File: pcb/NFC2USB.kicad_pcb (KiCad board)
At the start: 4 copper layers, 39 x 40 mm, 44 parts, among them J1 USB_C_USB2.0, SW1 BOOTSEL, SW2 MODE, U1 NFCModuleRC522, U2 AMS1117-3.3, U3 W25Q32JVSS, U4 RP2040, Y1 12MHz

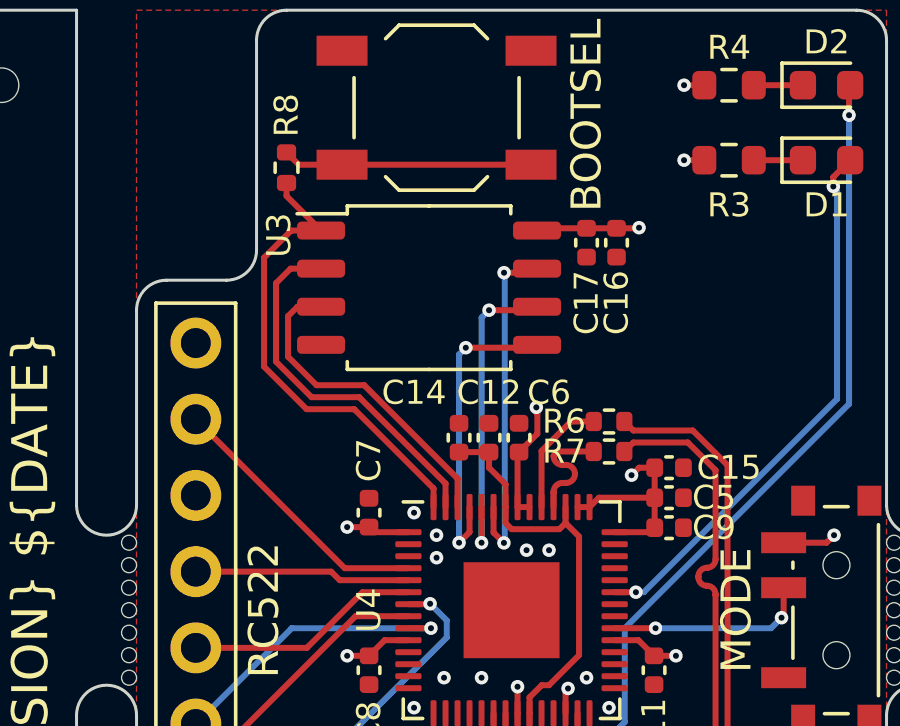
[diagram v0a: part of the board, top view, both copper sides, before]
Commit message: feat: change flash footprint
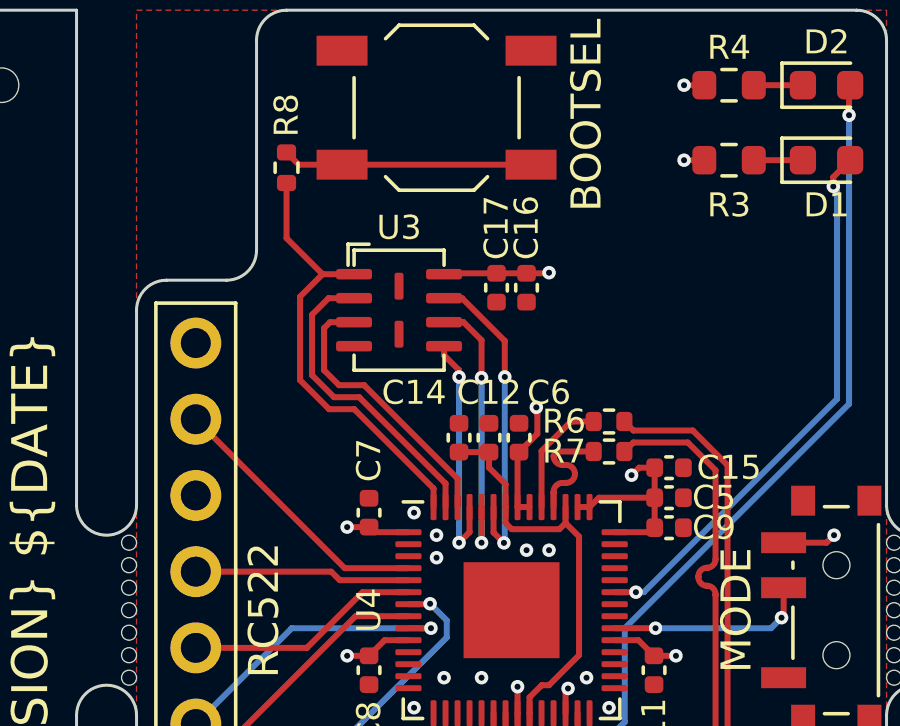
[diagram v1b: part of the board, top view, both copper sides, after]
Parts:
- U3: value W25Q32JVSS -> W25Q32JVUU; footprint Package_SO:SOIC-8_5.23x5.23mm_P1.27mm -> My_Footprints:USON8 (3x4)
- moved C16 3.35 mm to (113.0, 59.2)
- moved C17 3.35 mm to (112.0, 59.2)
- moved U3 1.25 mm to (108.8, 60.0), turned to -90 degrees
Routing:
- net /RP2040/QSPI_SD0: track 10.3 -> 8.09 mm
- net /RP2040/QSPI_SD1: track 12.4 -> 10.4 mm
- net /RP2040/QSPI_SD2: track 10.9 -> 9.38 mm
- net /RP2040/QSPI_SCLK: track 10.7 -> 9.44 mm
- net /RP2040/QSPI_SS: track 15.9 -> 15.0 mm
- net /RP2040/QSPI_SD3: track 11.5 -> 10.7 mm

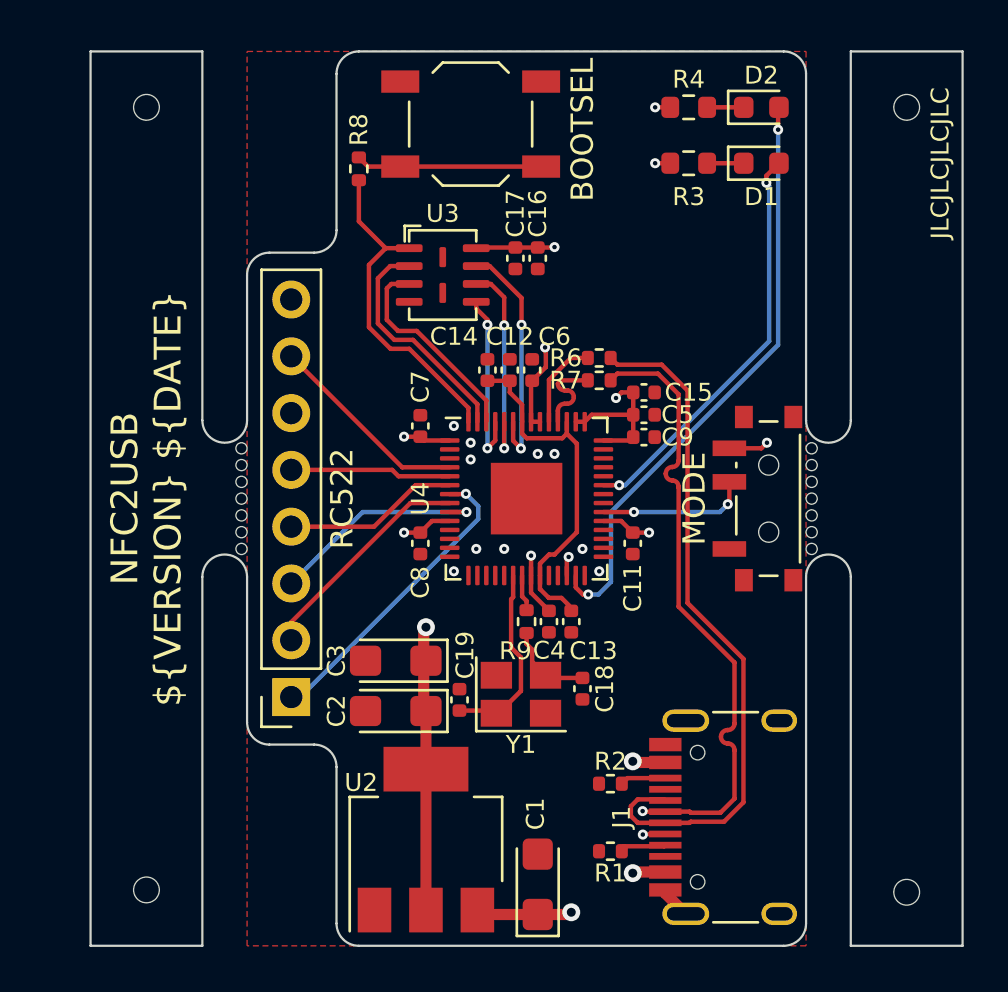
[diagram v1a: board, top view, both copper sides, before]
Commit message: style: move LEDs
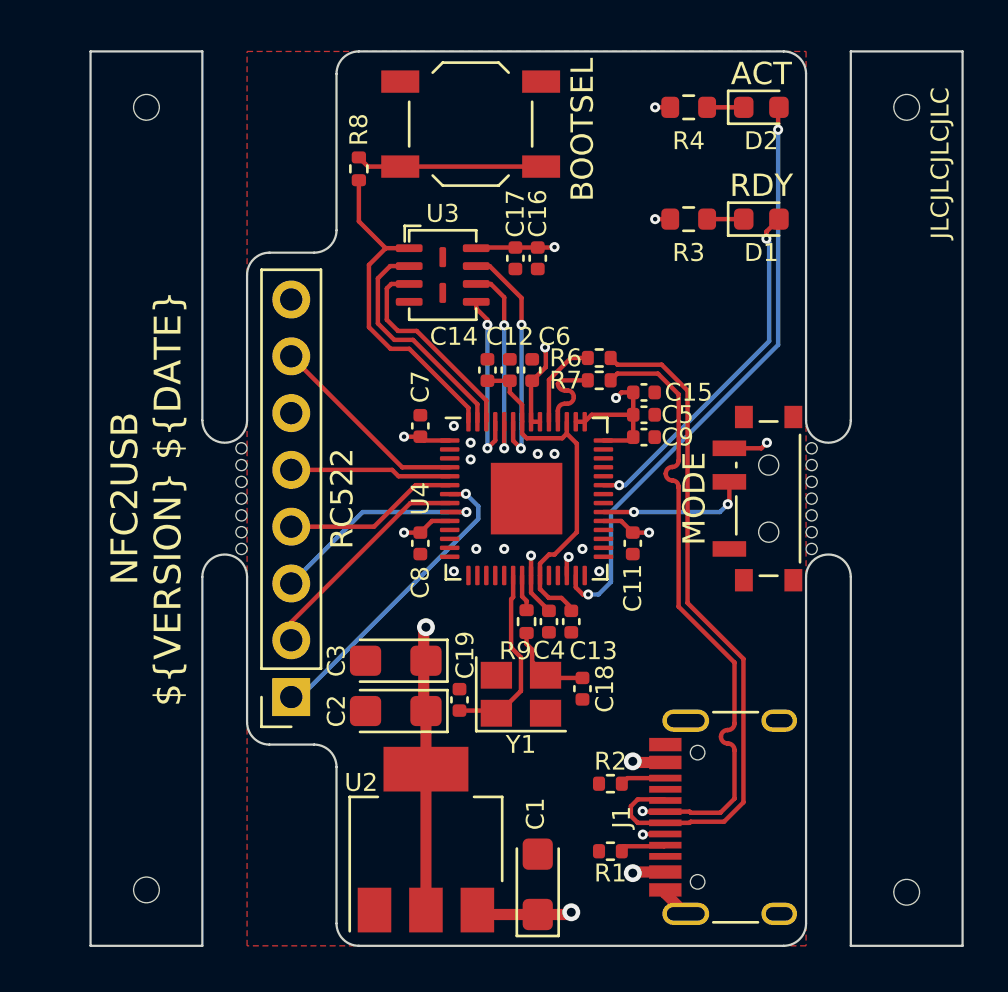
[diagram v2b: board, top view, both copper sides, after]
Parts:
- moved D1 2.50 mm to (123.0, 57.5)
- moved R3 2.50 mm to (119.8, 57.5)
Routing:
- net /LED_RDY: track 18.3 -> 15.8 mm
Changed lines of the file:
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@@
   )
   (footprint "LED_SMD:LED_0603_1608Metric" (layer "F.Cu")
-    (at 123 55)
+    (at 123 57.5)
     (descr "LED SMD 0603 (1608 Metric), square (rectangular) end terminal, IPC_7351 nominal, (Body size source: http://www.tortai-tech.com/upload/download/2011102023233369053.pdf), generated with kicad-footprint-generator")
     (tags "LED")
@@
       (effects (font (size 0.8 0.8) (thickness 0.15)))
     )
-    (fp_text value "RDY" (at 0 1.43) (layer "F.Fab")
+    (fp_text value "RDY" (at 0 -1.5 180) (layer "F.SilkS")
       (effects (font (size 1 1) (thickness 0.15)))
     )
@@
   )
   (footprint "Resistor_SMD:R_0603_1608Metric" (layer "F.Cu")
-    (at 119.75 55 180)
+    (at 119.75 57.5 180)
     (descr "Resistor SMD 0603 (1608 Metric), square (rectangular) end terminal, IPC_7351 nominal, (Body size source: IPC-SM-782 page 72, https://www.pcb-3d.com/wordpress/wp-content/uploads/ipc-sm-782a_amendment_1_and_2.pdf), generated with kicad-footprint-generator")
     (tags "resistor")
@@
     (property "Sheetname" "")
     (attr smd)
-    (fp_text reference "D2" (at 0 -1.43) (layer "F.SilkS")
+    (fp_text reference "D2" (at 0 1.5) (layer "F.SilkS")
       (effects (font (size 0.8 0.8) (thickness 0.15)))
     )
-    (fp_text value "ACT" (at 0 1.43) (layer "F.Fab")
+    (fp_text value "ACT" (at 0 -1.5 180) (layer "F.SilkS")
       (effects (font (size 1 1) (thickness 0.15)))
     )
@@
     (property "Sheetname" "")
     (attr smd)
-    (fp_text reference "R4" (at 0 1.25) (layer "F.SilkS")
+    (fp_text reference "R4" (at 0 -1.5) (layer "F.SilkS")
       (effects (font (size 0.8 0.8) (thickness 0.15)))
     )
@@
   (segment (start 118.705 87.5) (end 118.705 87.655) (width 0.5) (layer "F.Cu") (net 2))
   (segment (start 118.705 87.655) (end 119.62 88.57) (width 0.5) (layer "F.Cu") (net 2))
-  (segment (start 118.925 55) (end 118.25 55) (width 0.2) (layer "F.Cu") (net 2))
+  (segment (start 118.925 57.5) (end 118.25 57.5) (width 0.2) (layer "F.Cu") (net 2))
   (via (at 110 68.25) (size 0.45) (drill 0.2) (layers "F.Cu" "B.Cu") (free) (net 2))
   (via (at 113 68) (size 0.45) (drill 0.2) (layers "F.Cu" "B.Cu") (free) (net 2))
@@
   (via (at 109.25 66.75) (size 0.45) (drill 0.2) (layers "F.Cu" "B.Cu") (free) (net 2))
   (via (at 115 72.25) (size 0.45) (drill 0.2) (layers "F.Cu" "B.Cu") (free) (net 2))
-  (via (at 118.25 55) (size 0.45) (drill 0.2) (layers "F.Cu" "B.Cu") (net 2))
+  (via (at 118.25 57.5) (size 0.45) (drill 0.2) (layers "F.Cu" "B.Cu") (net 2))
   (via (at 111.5 72.25) (size 0.45) (drill 0.2) (layers "F.Cu" "B.Cu") (free) (net 2))
   (via (at 109.25 73.25) (size 0.45) (drill 0.2) (layers "F.Cu" "B.Cu") (free) (net 2))
@@
   (segment (start 117.472537 83.4505) (end 117.165 83.758037) (width 0.2) (layer "F.Cu") (net 8))
   (segment (start 118.6555 83.4505) (end 117.472537 83.4505) (width 0.2) (layer "F.Cu") (net 8))
-  (segment (start 120.575 55) (end 122.2125 55) (width 0.2) (layer "F.Cu") (net 9))
+  (segment (start 120.575 57.5) (end 122.2125 57.5) (width 0.2) (layer "F.Cu") (net 9))
   (segment (start 120.575 52.5) (end 122.2125 52.5) (width 0.2) (layer "F.Cu") (net 10))
   (segment (start 118.705 85.5) (end 118.6555 85.5495) (width 0.2) (layer "F.Cu") (net 11))
@@
   (segment (start 112.5 74.575674) (end 112.3 74.375674) (width 0.2) (layer "F.Cu") (net 16))
   (segment (start 112.5 74.99) (end 112.5 74.575674) (width 0.2) (layer "F.Cu") (net 16))
-  (segment (start 123.2255 55.562) (end 123.7875 55) (width 0.2) (layer "F.Cu") (net 17))
+  (segment (start 123.2255 58.062) (end 123.7875 57.5) (width 0.2) (layer "F.Cu") (net 17))
   (segment (start 116.645391 69.4) (end 115.9375 69.4) (width 0.2) (layer "F.Cu") (net 17))
-  (segment (start 123.2255 55.8755) (end 123.2255 55.562) (width 0.2) (layer "F.Cu") (net 17))
-  (via (at 123.2255 55.8755) (size 0.45) (drill 0.2) (layers "F.Cu" "B.Cu") (net 17))
+  (segment (start 123.2255 58.3755) (end 123.2255 58.062) (width 0.2) (layer "F.Cu") (net 17))
+  (via (at 123.2255 58.3755) (size 0.45) (drill 0.2) (layers "F.Cu" "B.Cu") (net 17))
   (via (at 116.645391 69.4) (size 0.45) (drill 0.2) (layers "F.Cu" "B.Cu") (net 17))
-  (segment (start 123.2255 55.8755) (end 123.35 56) (width 0.2) (layer "B.Cu") (net 17))
-  (segment (start 116.910527 69.4) (end 116.645391 69.4) (width 0.2) (layer "B.Cu") (net 17))
-  (segment (start 123.35 62.960527) (end 116.910527 69.4) (width 0.2) (layer "B.Cu") (net 17))
-  (segment (start 123.35 56) (end 123.35 62.960527) (width 0.2) (layer "B.Cu") (net 17))
+  (segment (start 116.910527 69.4) (end 123.35 62.960527) (width 0.2) (layer "B.Cu") (net 17))
+  (segment (start 123.35 58.5) (end 123.2255 58.3755) (width 0.2) (layer "B.Cu") (net 17))
+  (segment (start 116.645391 69.4) (end 116.910527 69.4) (width 0.2) (layer "B.Cu") (net 17))
+  (segment (start 123.35 62.960527) (end 123.35 58.5) (width 0.2) (layer "B.Cu") (net 17))
   (segment (start 115.016912 74.286887) (end 114.7 73.969975) (width 0.2) (layer "F.Cu") (net 18))
   (segment (start 123.75 53.5) (end 123.75 52.5375) (width 0.2) (layer "F.Cu") (net 18))
@@
   (via (at 123.75 53.5) (size 0.45) (drill 0.2) (layers "F.Cu" "B.Cu") (net 18))
   (via (at 115.258679 74.286887) (size 0.45) (drill 0.2) (layers "F.Cu" "B.Cu") (net 18))
-  (segment (start 116.275 70.601213) (end 116.275 73.725) (width 0.2) (layer "B.Cu") (net 18))
-  (segment (start 123.75 53.5) (end 123.75 63.126213) (width 0.2) (layer "B.Cu") (net 18))
-  (segment (start 116.275 73.725) (end 115.713113 74.286887) (width 0.2) (layer "B.Cu") (net 18))
-  (segment (start 115.713113 74.286887) (end 115.258679 74.286887) (width 0.2) (layer "B.Cu") (net 18))
-  (segment (start 123.75 63.126213) (end 116.275 70.601213) (width 0.2) (layer "B.Cu") (net 18))
+  (segment (start 123.75 63.126213) (end 123.75 53.5) (width 0.2) (layer "B.Cu") (net 18))
+  (segment (start 116.275 73.725) (end 116.275 70.601213) (width 0.2) (layer "B.Cu") (net 18))
+  (segment (start 115.258679 74.286887) (end 115.713113 74.286887) (width 0.2) (layer "B.Cu") (net 18))
+  (segment (start 115.713113 74.286887) (end 116.275 73.725) (width 0.2) (layer "B.Cu") (net 18))
+  (segment (start 116.275 70.601213) (end 123.75 63.126213) (width 0.2) (layer "B.Cu") (net 18))
   (segment (start 106.4 59.6) (end 107.25 59.6) (width 0.2) (layer "F.Cu") (net 19))
   (segment (start 107.42206 62.9) (end 106.584314 62.9) (width 0.2) (layer "F.Cu") (net 19))

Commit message: style: update Titles
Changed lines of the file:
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@@
   (paper "A4")
   (title_block
-    (title "NFC2USB")
+    (title "Bloop NFC Scanner")
     (date "${DATE}")
     (rev "${VERSION}")
@@
   )
   (gr_text "${TITLE}\n${VERSION} ${DATE}" (at 120.5 70 90) (layer "B.SilkS")
-    (effects (font (size 1.5 1.5) (thickness 0.2)) (justify mirror))
+    (effects (font (size 1.5 1.2) (thickness 0.2)) (justify mirror))
   )
   (gr_text "3V3" (at 103.5 61.1) (layer "B.SilkS")

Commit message: feat: add silkscreen to LEDs and switch
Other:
- board text added: "ACTIVE"
- board text added: "HOTKEY"
- board text added: "PLAIN"
- board text added: "READY"
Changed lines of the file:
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@@
       (effects (font (size 0.8 0.8) (thickness 0.15)))
     )
-    (fp_text value "RDY" (at 0 -1.5 180) (layer "F.SilkS")
+    (fp_text value "RDY" (at 0 -1.5 180) (layer "F.Fab")
       (effects (font (size 1 1) (thickness 0.15)))
     )
@@
       (effects (font (size 0.8 0.8) (thickness 0.15)))
     )
-    (fp_text value "ACT" (at 0 -1.5 180) (layer "F.SilkS")
+    (fp_text value "ACT" (at 0 -1.5 180) (layer "F.Fab")
       (effects (font (size 1 1) (thickness 0.15)))
     )
@@
     (effects (font (size 1.2 1.2) (thickness 0.18)))
   )
+  (gr_text "HOTKEY" (at 124.25 62.75 90) (layer "F.SilkS")
+    (effects (font (size 1 1) (thickness 0.15)))
+  )
+  (gr_text "PLAIN" (at 124.25 76.5 90) (layer "F.SilkS")
+    (effects (font (size 1 1) (thickness 0.15)))
+  )
+  (gr_text "READY" (at 122.25 56) (layer "F.SilkS")
+    (effects (font (size 1 1) (thickness 0.15)))
+  )
   (gr_text "JLCJLCJLCJLC" (at 131 55 90) (layer "F.SilkS")
     (effects (font (size 0.8 0.8) (thickness 0.15)))
   )
+  (gr_text "ACTIVE" (at 122.25 51) (layer "F.SilkS")
+    (effects (font (size 1 1) (thickness 0.15)))
+  )
   (gr_text "BOOTSEL" (at 115 53.5 90) (layer "F.SilkS")

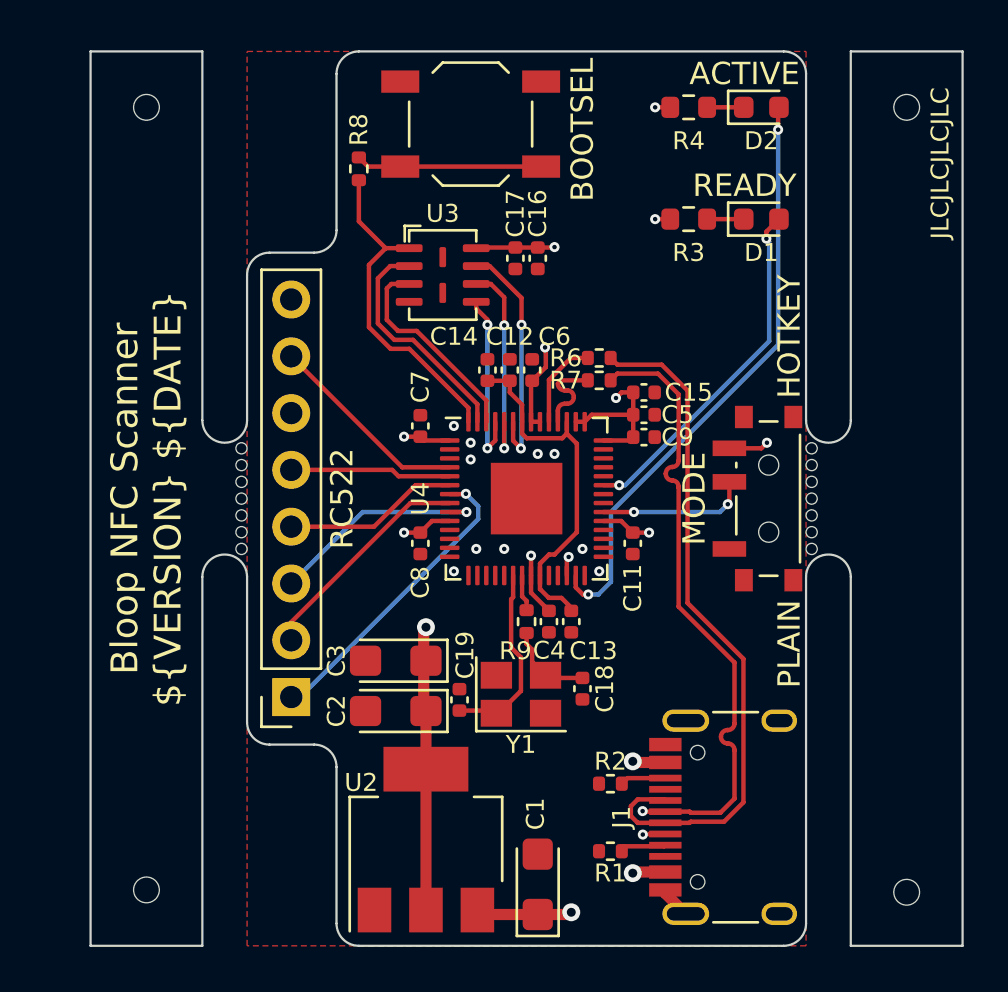
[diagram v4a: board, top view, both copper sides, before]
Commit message: fix: move mouse bites away from mode switch
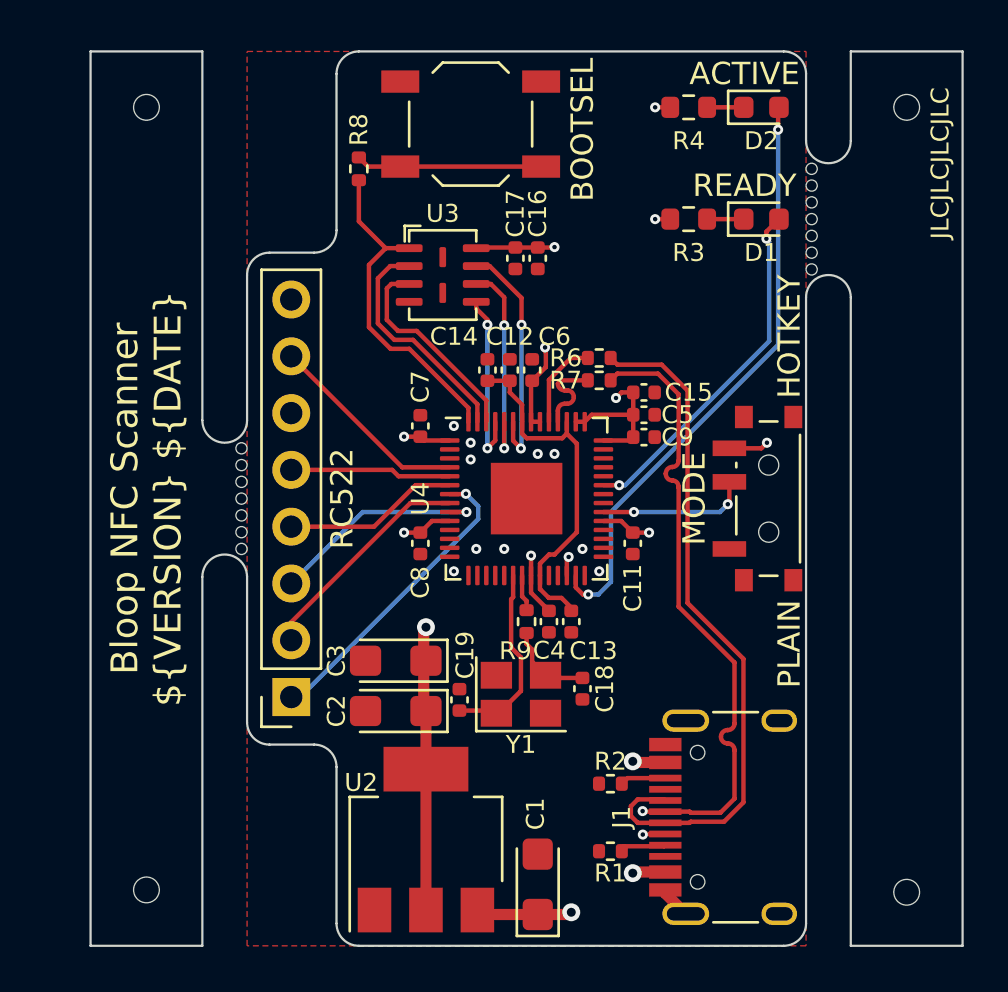
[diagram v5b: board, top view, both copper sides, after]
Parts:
- moved mouse-bite-2mm-slot 12.5 mm to (126.0, 57.5)
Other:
- outline, holes or cut-outs redrawn
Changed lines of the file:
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@@
   )
   (footprint "Panelization:mouse-bite-2x5mm-slot-onesided" (layer "F.Cu")
-    (at 126 70 90)
+    (at 126 57.5 90)
     (attr board_only exclude_from_pos_files exclude_from_bom)
     (fp_text reference "mouse-bite-2mm-slot" (at 0 -2 90) (layer "F.SilkS") hide
@@
   (gr_line (start 104 82) (end 104 89) (layer "Edge.Cuts") (width 0.1))
   (gr_line (start 104 51) (end 104 58) (layer "Edge.Cuts") (width 0.1))
-  (gr_line (start 127 66.5) (end 127 50) (layer "Edge.Cuts") (width 0.1))
+  (gr_line (start 127 54) (end 127 50) (layer "Edge.Cuts") (width 0.1))
   (gr_arc (start 105 90) (mid 104.292893 89.707107) (end 104 89) (layer "Edge.Cuts") (width 0.1))
   (gr_line (start 124 90) (end 105 90) (layer "Edge.Cuts") (width 0.1))
@@
   (gr_line (start 103 59) (end 101 59) (layer "Edge.Cuts") (width 0.1))
   (gr_arc (start 124 50) (mid 124.707107 50.292893) (end 125 51) (layer "Edge.Cuts") (width 0.1))
-  (gr_line (start 125 51) (end 125 66.5) (layer "Edge.Cuts") (width 0.1))
+  (gr_line (start 125 51) (end 125 54) (layer "Edge.Cuts") (width 0.1))
   (gr_arc (start 104 58) (mid 103.707107 58.707107) (end 103 59) (layer "Edge.Cuts") (width 0.1))
   (gr_arc (start 104 51) (mid 104.292893 50.292893) (end 105 50) (layer "Edge.Cuts") (width 0.1))
-  (gr_line (start 125 73.5) (end 125 89) (layer "Edge.Cuts") (width 0.1))
+  (gr_line (start 125 61) (end 125 89) (layer "Edge.Cuts") (width 0.1))
   (gr_arc (start 125 89) (mid 124.707107 89.707107) (end 124 90) (layer "Edge.Cuts") (width 0.1))
   (gr_line (start 101 81) (end 103 81) (layer "Edge.Cuts") (width 0.1))
   (gr_line (start 93 90) (end 98 90) (layer "Edge.Cuts") (width 0.1))
-  (gr_line (start 127 90) (end 127 73.5) (layer "Edge.Cuts") (width 0.1))
+  (gr_line (start 127 90) (end 127 61) (layer "Edge.Cuts") (width 0.1))
   (gr_line (start 98 50) (end 93 50) (layer "Edge.Cuts") (width 0.1))
   (gr_arc (start 103 81) (mid 103.707107 81.292893) (end 104 82) (layer "Edge.Cuts") (width 0.1))
